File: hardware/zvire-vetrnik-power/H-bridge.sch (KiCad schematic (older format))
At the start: 46 parts, among them J6 DC IN, J7 PE, J8 CURRENT SENSOR, J9 AC OUT, Q10 IXFP90N20X3M, Q11 IXFP90N20X3M, Q12 IXFP90N20X3M, Q8 BC846, Q9 IXFP90N20X3M, U5 LM393, U6 IR2104, U7 IR2104

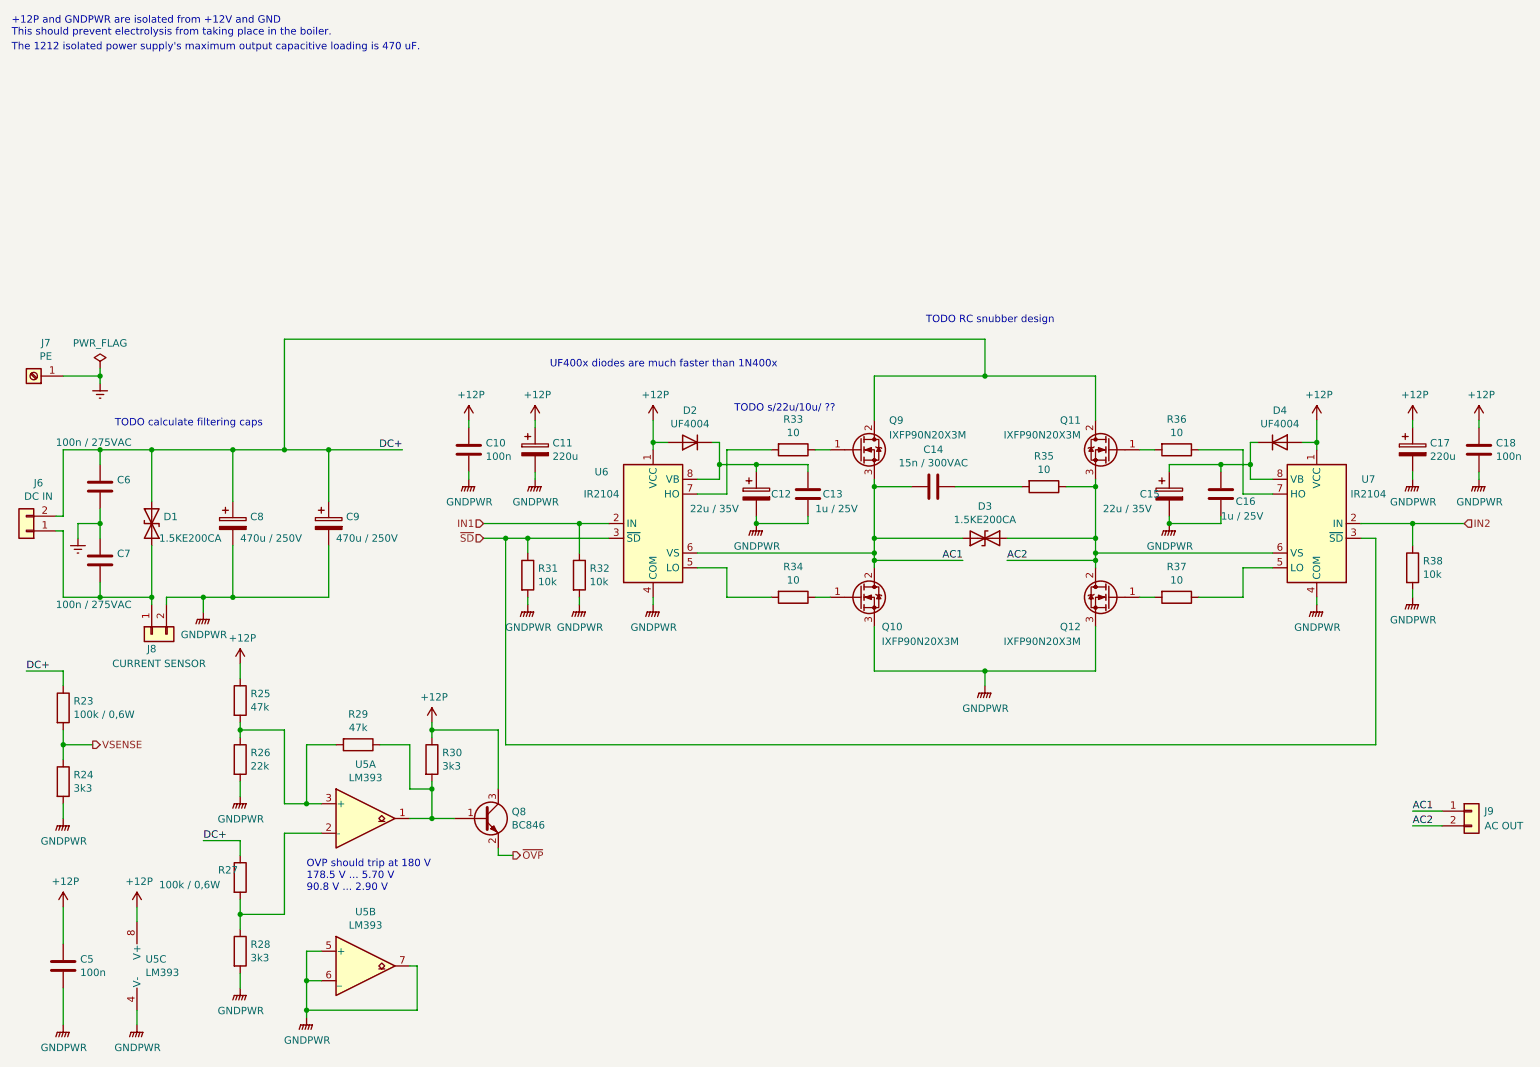
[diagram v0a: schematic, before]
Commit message: Vyrobena verze power PCB
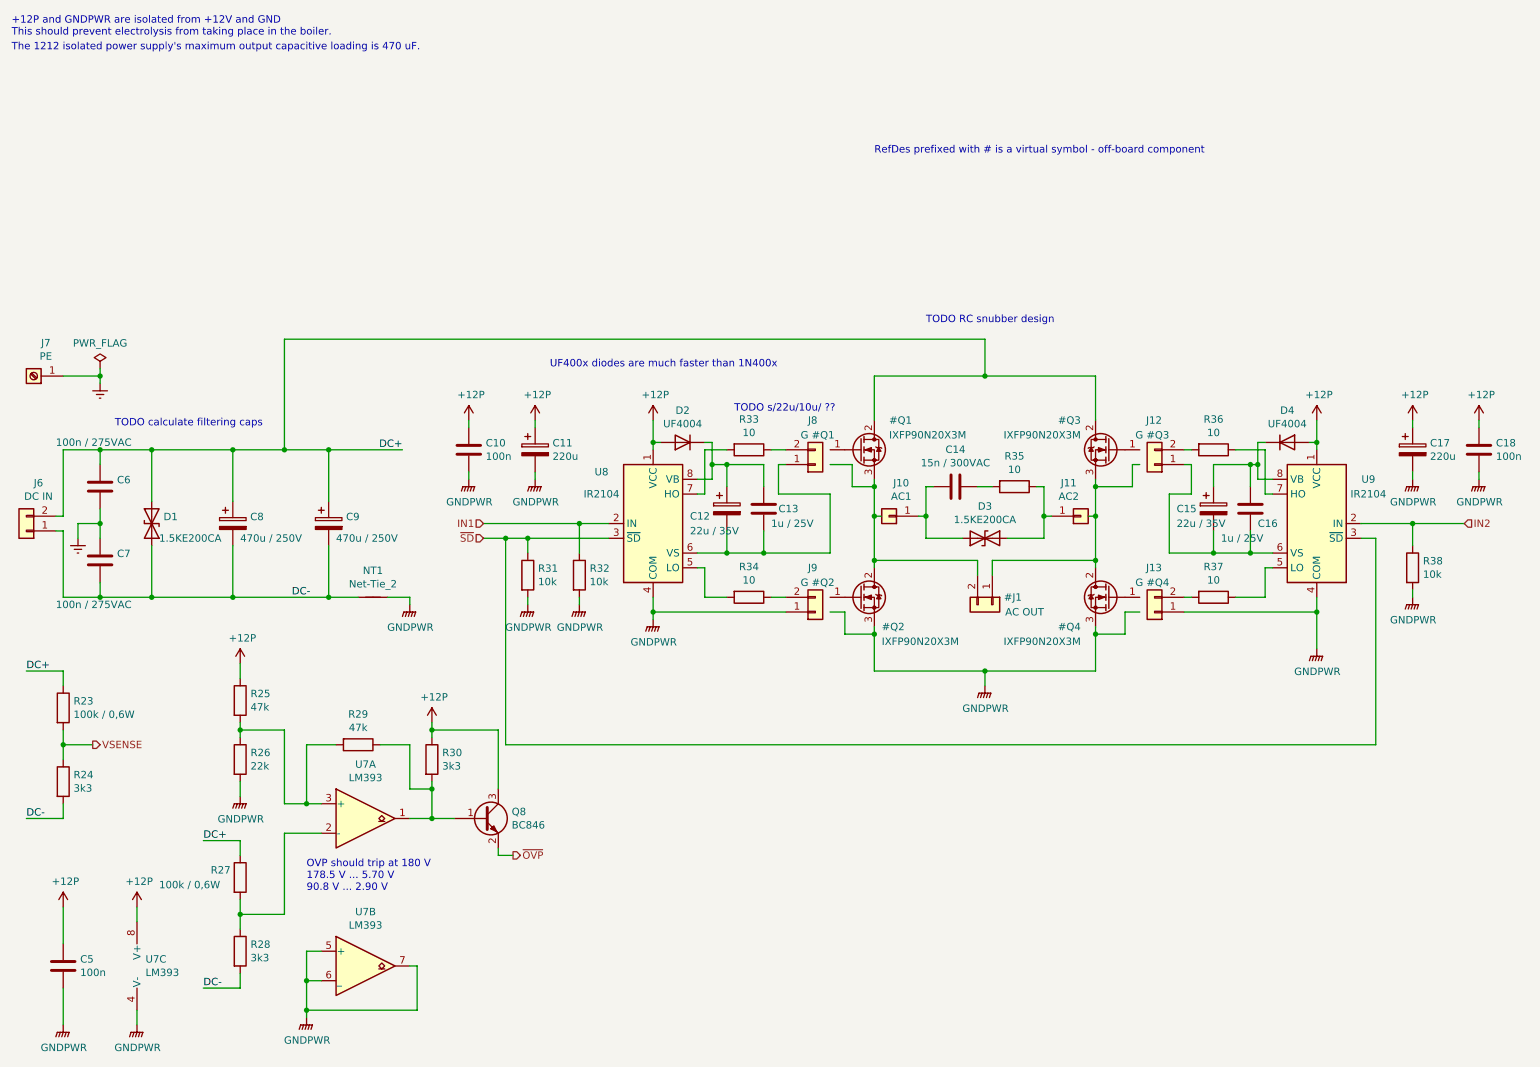
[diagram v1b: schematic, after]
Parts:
- removed Q10, Q11, Q12, Q9: IXFP90N20X3M, Package_TO_SOT_THT:TO-220F-3_Vertical, symbol ondra:IXFP90N20X3M
- added J10: AC1, ondra:FS1536, symbol Connector_Generic:Conn_01x01
- added J11: AC2, ondra:FS1536, symbol Connector_Generic:Conn_01x01
- added J12: G #Q3, Connector_Molex:Molex_KK-254_AE-6410-02A_1x02_P2.54mm_Vertical, symbol Connector_Generic:Conn_01x02
- added J13: G #Q4, Connector_Molex:Molex_KK-254_AE-6410-02A_1x02_P2.54mm_Vertical, symbol Connector_Generic:Conn_01x02
- added NT1: Net-Tie_2, NetTie:NetTie-2_SMD_Pad2.0mm, symbol Device:Net-Tie_2
- J8: value CURRENT SENSOR -> G #Q1; footprint ondra:DG270-10.0-02P-14-00A -> Connector_Molex:Molex_KK-254_AE-6410-02A_1x02_P2.54mm_Vertical
- J9: value AC OUT -> G #Q2; footprint ondra:DG270-10.0-02P-14-00A -> Connector_Molex:Molex_KK-254_AE-6410-02A_1x02_P2.54mm_Vertical; TME https://www.tme.eu/cz/details/dg270-10.0-02p/svorkovnice-do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 -> (none)
- renumbered U5 to U7, U6 to U8, U7 to U9
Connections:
- net labels added: AC OUT, DC-, IXFP90N20X3M
- net labels removed: AC1, AC2
- wire segments 186 -> 221
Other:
- note added: "RefDes prefixed with # is a virtual symbol - off-board component"
- moved on the sheet: C12, C13, C14, C15, C16, D2, D4, R33, R34, R35, R36, R37
